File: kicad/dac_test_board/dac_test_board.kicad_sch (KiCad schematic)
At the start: 29 parts, among them J10 Data_In, J2 Vcca_select, J3 Data_Out, J7 Vccb_select, U2 SN74LVC8T245

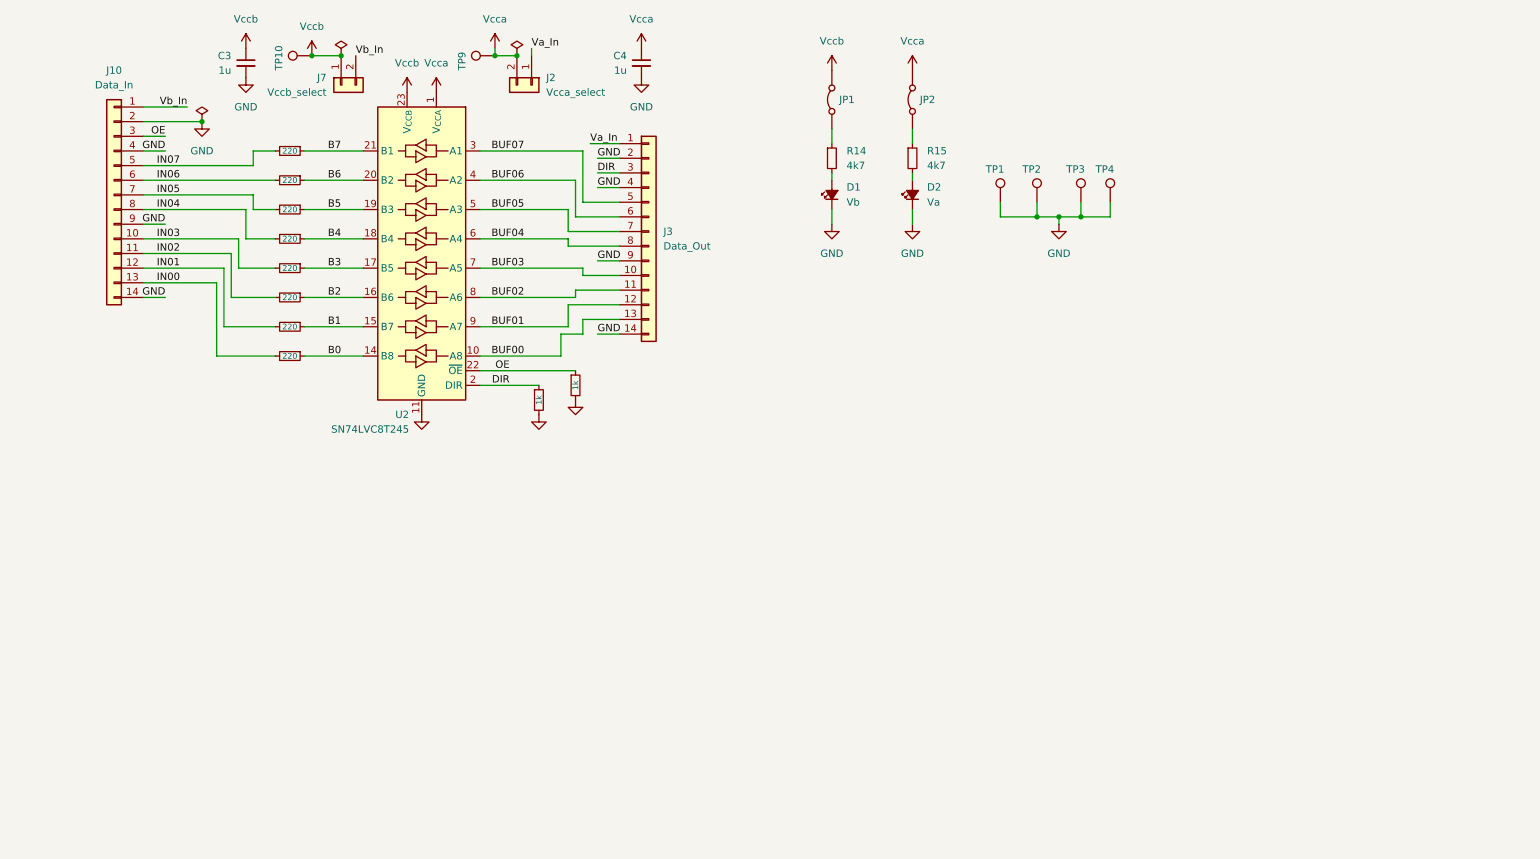
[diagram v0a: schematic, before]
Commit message: renamed files, was working on wrong directory
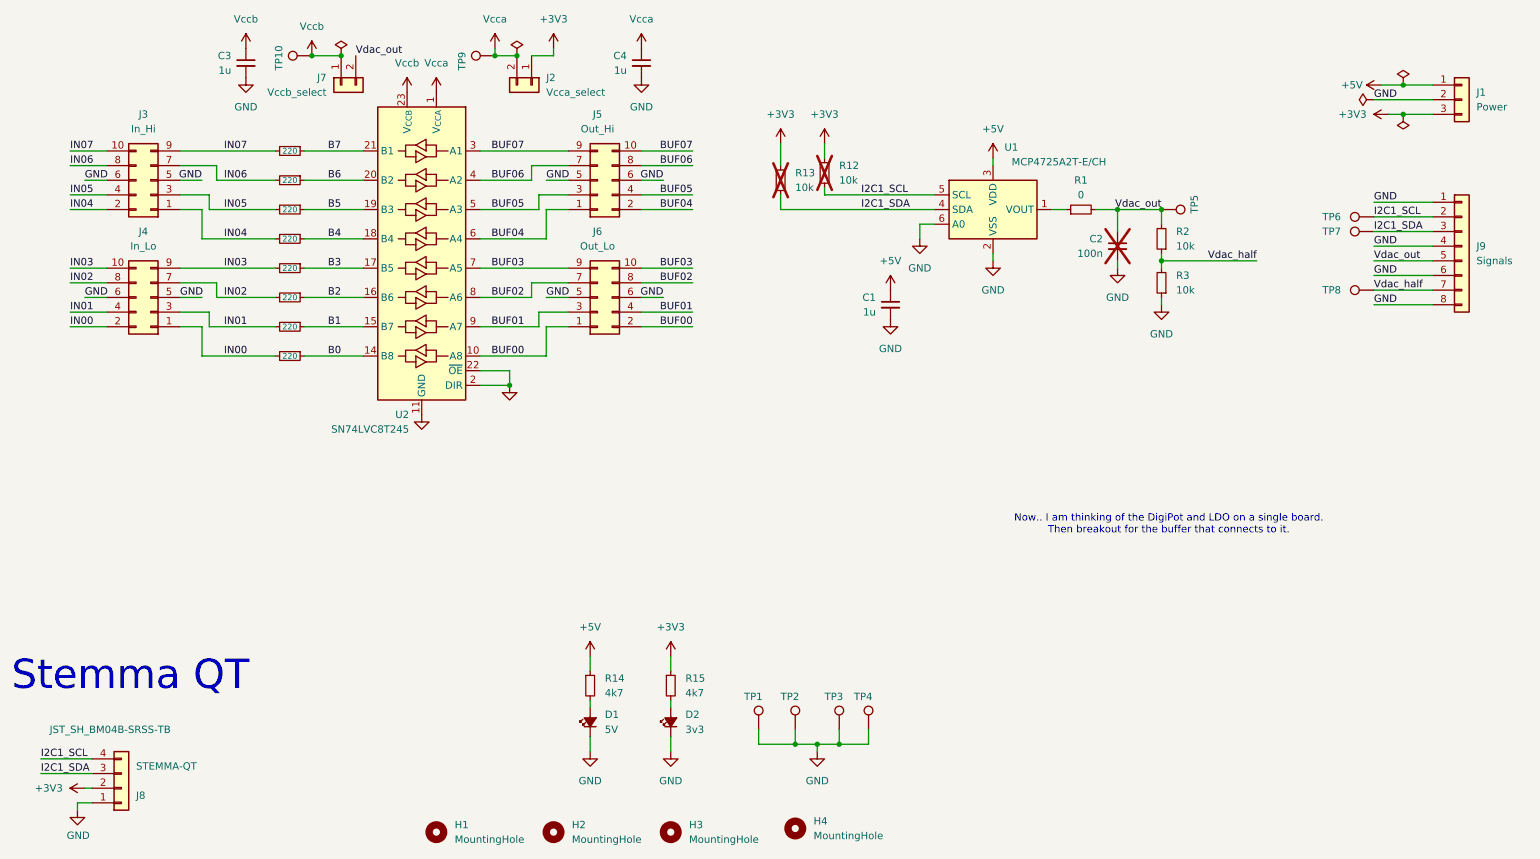
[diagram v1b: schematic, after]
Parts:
- removed J10: Data_In, Connector_PinHeader_2.54mm:PinHeader_1x14_P2.54mm_Vertical, symbol Connector_Generic:Conn_01x14
- removed J3: Data_Out, Connector_PinHeader_2.54mm:PinHeader_1x14_P2.54mm_Vertical, symbol Connector_Generic:Conn_01x14
- removed JP1, JP2: Jumper_2_Bridged, Jumper:SolderJumper-2_P1.3mm_Bridged_RoundedPad1.0x1.5mm, symbol Jumper:Jumper_2_Bridged
- added C1: 1u, Capacitor_SMD:C_0603_1608Metric_Pad1.08x0.95mm_HandSolder, symbol Device:C_Small
- added C2: 100n, Capacitor_SMD:C_0603_1608Metric_Pad1.08x0.95mm_HandSolder, symbol Device:C_Small
- added H1, H2, H3, H4: MountingHole, MountingHole:MountingHole_2.7mm, symbol Mechanical:MountingHole
- added J1: Power, Connector_PinHeader_2.54mm:PinHeader_1x03_P2.54mm_Vertical, symbol Connector_Generic:Conn_01x03
- added J3: In_Hi, Connector_PinHeader_2.54mm:PinHeader_2x05_P2.54mm_Vertical, symbol Connector_Generic:Conn_02x05_Odd_Even
- added J4: In_Lo, Connector_PinHeader_2.54mm:PinHeader_2x05_P2.54mm_Vertical, symbol Connector_Generic:Conn_02x05_Odd_Even
- added J5: Out_Hi, Connector_PinHeader_2.54mm:PinHeader_2x05_P2.54mm_Vertical, symbol Connector_Generic:Conn_02x05_Odd_Even
- added J6: Out_Lo, Connector_PinHeader_2.54mm:PinHeader_2x05_P2.54mm_Vertical, symbol Connector_Generic:Conn_02x05_Odd_Even
- added J8: JST_SH_BM04B-SRSS-TB, Connector_JST:JST_SH_BM04B-SRSS-TB_1x04-1MP_P1.00mm_Vertical, symbol Connector_Generic:Conn_01x04
- added J9: Signals, Connector_PinHeader_2.54mm:PinHeader_1x08_P2.54mm_Vertical, symbol Connector_Generic:Conn_01x08
- added R12, R13, R3: 10k, Resistor_SMD:R_0603_1608Metric, symbol Device:R_Small
- added TP5, TP6, TP7, TP8: TestPoint_Harwin, My Libraries:Harwin-S1751-46-Test-Point, symbol My Library:TestPoint_Harwin
- added U1: MCP4725A2T-E/CH, Package_TO_SOT_SMD:SOT-23-6, symbol Analog_DAC:MCP4725xxx-xCH
- D1: value Vb -> 5V
- D2: value Va -> 3v3
- R1: value 1k -> 0
- R2: value 1k -> 10k
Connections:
- net Va_In is gone; now on net +3V3: J2.1 (Pin_1)
- net BUF00: now also J6.1 (Pin_1), J6.2 (Pin_2)
- net BUF01: now also J6.3 (Pin_3), J6.4 (Pin_4)
- net BUF02: now also J6.7 (Pin_7), J6.8 (Pin_8)
- net BUF03: now also J6.10 (Pin_10), J6.9 (Pin_9)
- net BUF04: now also J5.1 (Pin_1), J5.2 (Pin_2)
- net BUF05: now also J5.3 (Pin_3), J5.4 (Pin_4)
- net BUF06: now also J5.7 (Pin_7), J5.8 (Pin_8)
- net BUF07: now also J5.10 (Pin_10), J5.9 (Pin_9)
- net GND: now also U2.2 (DIR), U2.22 (~{OE}), C1.2, C2.2, J1.2 (Pin_2), J3.5 (Pin_5), J3.6 (Pin_6), J4.5 (Pin_5), J4.6 (Pin_6), J5.5 (Pin_5), J5.6 (Pin_6), J6.5 (Pin_5), J6.6 (Pin_6), J8.1 (Pin_1), J9.1 (Pin_1), J9.4 (Pin_4), J9.6 (Pin_6), J9.8 (Pin_8), R3.1, U1.2 (VSS), U1.6 (A0); no longer R1.2, R2.2
- net IN00: now also J4.1 (Pin_1), J4.2 (Pin_2)
- net IN01: now also J4.3 (Pin_3), J4.4 (Pin_4)
- net IN02: now also J4.7 (Pin_7), J4.8 (Pin_8)
- net IN03: now also J4.10 (Pin_10), J4.9 (Pin_9)
- net IN04: now also J3.1 (Pin_1), J3.2 (Pin_2)
- net IN05: now also J3.3 (Pin_3), J3.4 (Pin_4)
- net IN06: now also J3.7 (Pin_7), J3.8 (Pin_8)
- net IN07: now also J3.10 (Pin_10), J3.9 (Pin_9)
- net +5V: now reaches R14.1
- net +5V: now also C1.1, J1.1 (Pin_1), U1.3 (VDD)
- net +3V3: now reaches R15.1
- net +3V3: now also J1.3 (Pin_3), J8.2 (Pin_2), R12.2, R13.2
- net DIR: no longer names the net of R1.1
- net DIR: now also U1.1 (VOUT); no longer U2.2 (DIR)
- net OE renamed Vdac_half
- net Vdac_half: now also J9.7 (Pin_7), R3.2, TP8.1; no longer U2.22 (~{OE})
- net Vb_In renamed Vdac_out
- net Vdac_out: now also R1.2, R2.2, C2.1, J9.5 (Pin_5), TP5.1
- new net I2C1_SCL: J8.4 (Pin_4), J9.2 (Pin_2), R12.1, TP6.1, U1.5 (SCL)
- new net I2C1_SDA: J8.3 (Pin_3), J9.3 (Pin_3), R13.1, TP7.1, U1.4 (SDA)
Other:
- note added: "Now.. I am thinking of the DigiPot and LDO on a single board. Then breakout for the buffer that connects to it."
- note added: "Stemma QT"
- moved on the sheet: D1, D2, R14, R15, TP1, TP2, TP3, TP4
